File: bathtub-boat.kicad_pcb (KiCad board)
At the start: 2 copper layers, 61 x 35 mm, 54 parts, among them J1 I2C, J2 SPI, J3 I2C, J4 DS18B20, J5 1WireTRS, SW1 MODE, SW2 RESET, SW3 POWER, SW4 A, U1 esp-01m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

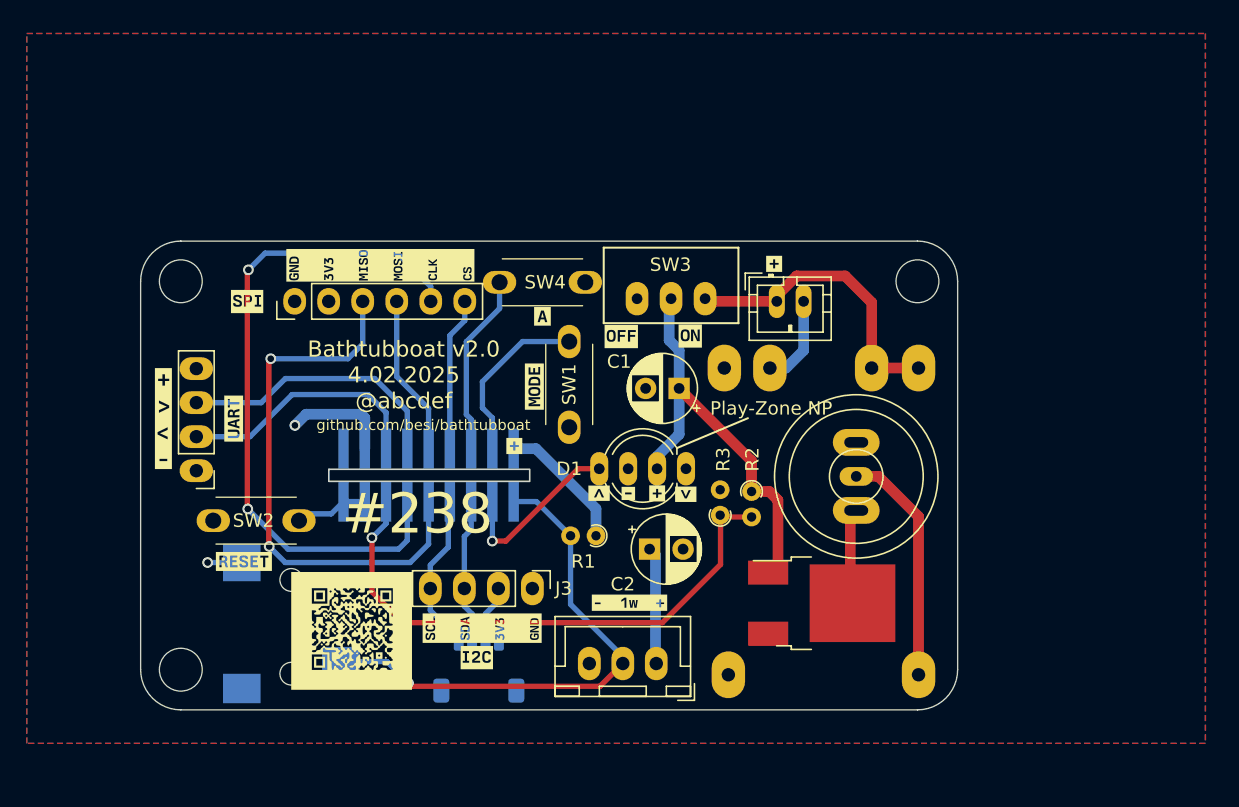
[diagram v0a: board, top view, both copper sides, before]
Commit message: Add a DS18B20 that is facing downwards in the center for under water placement
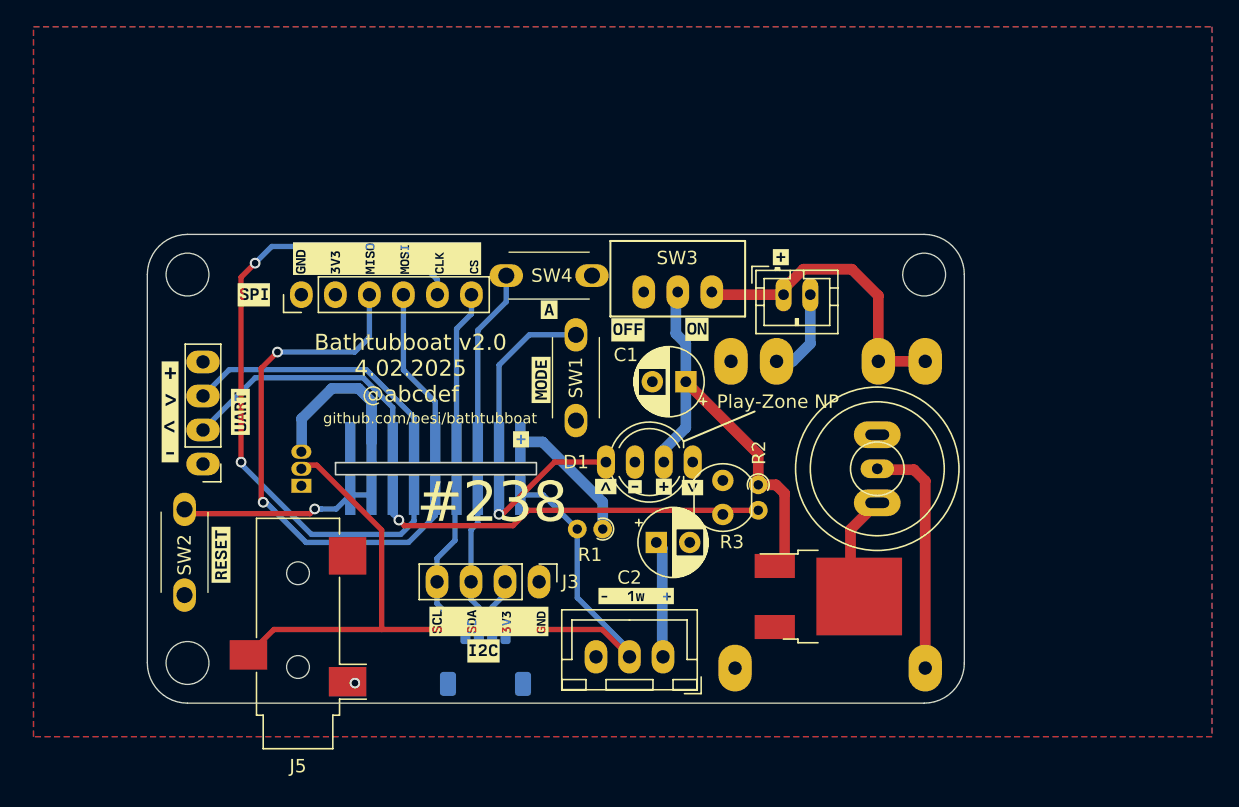
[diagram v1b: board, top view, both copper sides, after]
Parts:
- removed the G*** at (115.3, 94.6)
- added U4: DS18B20, Package_TO_SOT_THT:TO-92_Inline, B.Cu at (111.5, 83.8)
- added kibuzzard-65B8C757: G***, kibuzzard-65B8C757, B.Cu at (130.0, 68.1)
- J5: moved to F.Cu
- R3: value TODO Add Light meter here -> A1050; footprint Resistor_THT:R_Axial_DIN0204_L3.6mm_D1.6mm_P1.90mm_Vertical -> OptoDevice:R_LDR_4.9x4.2mm_P2.54mm_Vertical
- moved kibuzzard-65B79597 7.90 mm to (101.2, 88.8), turned to -90 degrees
- moved SW2 5.96 mm to (102.8, 91.9), turned to 90 degrees
- moved kibuzzard-65B79597 1.78 mm to (105.5, 88.9), turned to 90 degrees
- moved U6 1.67 mm to (154.5, 82.5)
- moved kibuzzard-65B7959E 0.92 mm to (132.0, 75.7), turned to -90 degrees
- moved kibuzzard-65D7C44D 0.75 mm to (107.0, 78.2), turned to -90 degrees
- moved BT3 0.71 mm to (147.5, 69.5)
- moved C1 0.71 mm to (140.2, 76.0)
- moved C2 0.71 mm to (138.0, 88.0)
- moved D1 0.71 mm to (140.7, 82.0)
- moved H1 0.71 mm to (103.0, 68.0)
- moved H2 0.71 mm to (158.0, 68.0)
- moved H3 0.71 mm to (103.0, 97.0)
- moved J1 0.71 mm to (125.2, 96.7)
- moved J2 0.71 mm to (111.5, 69.5)
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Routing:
- net Temp: track 39.0 -> 62.0 mm, vias 1 -> 0
- net ADC: track 42.0 -> 29.6 mm
- net Net-(U1-GP16): track 5.50 -> 14.7 mm, vias 0 -> 1
- net Neopixel: track 13.2 -> 11.1 mm
- net SPI_MISO: track 40.7 -> 38.8 mm
- net GND: track 7.18 -> 8.69 mm, vias 0 -> 1
- net SPI_CLK: track 50.5 -> 49.2 mm
- net +3V3: track 33.7 -> 35.0 mm, vias 2 -> 0
- net Net-(U1-GP0): track 13.0 -> 12.4 mm
- net TX: track 18.7 -> 19.3 mm

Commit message: Change resistors, improve silkscreen and add OSHW logo
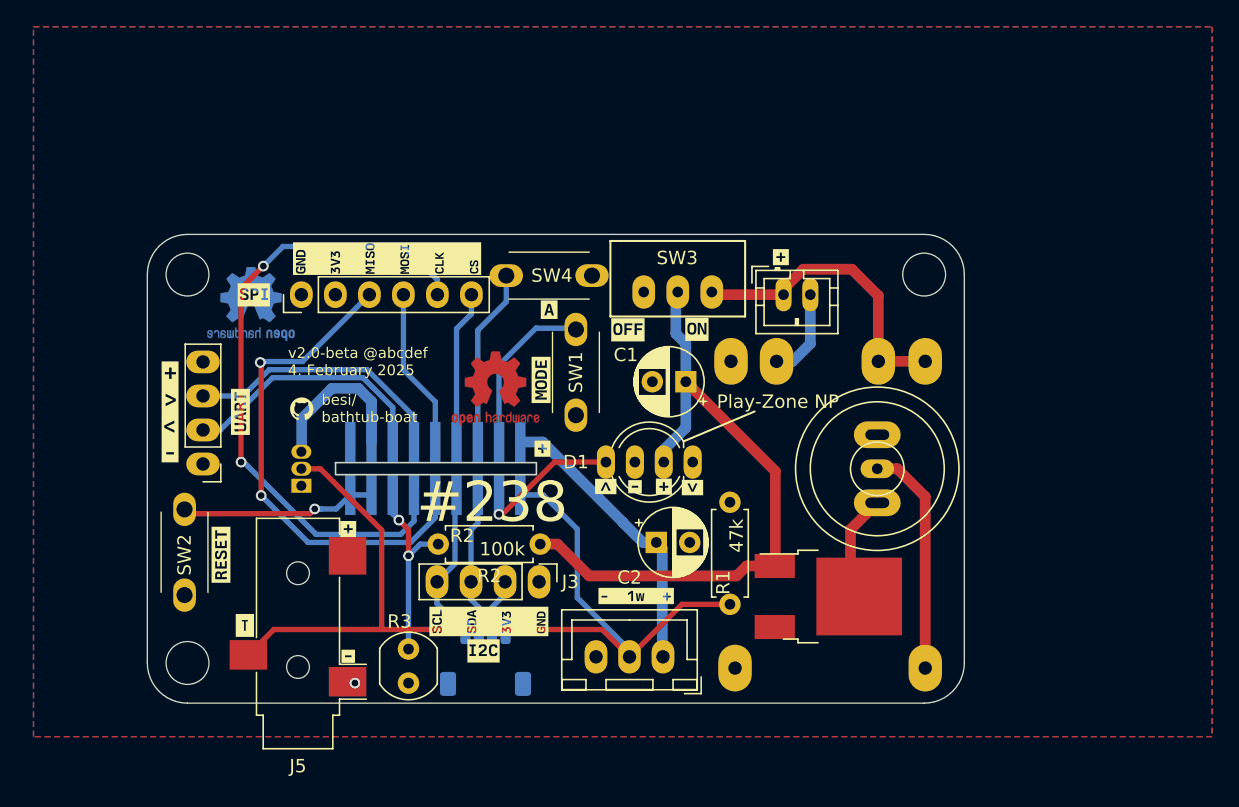
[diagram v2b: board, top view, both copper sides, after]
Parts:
- added G***: LOGO, LOGO, F.Cu at (111.5, 78.0)
- added REF**: OSHW-Logo2_7.3x6mm_Copper, Symbol:OSHW-Logo2_7.3x6mm_Copper, F.Cu at (126.0, 76.5)
- added REF**: OSHW-Logo2_7.3x6mm_Copper, Symbol:OSHW-Logo2_7.3x6mm_Copper, B.Cu at (107.7, 70.2)
- added kibuzzard-65B795B9: G***, kibuzzard-65B795B9, F.Cu at (115.0, 87.0)
- added kibuzzard-65D6F389: G***, kibuzzard-65D6F389, F.Cu at (115.0, 96.5)
- added kibuzzard-67A2929D: G***, kibuzzard-67A2929D, F.Cu at (107.3, 94.2)
- R1, R2: footprint Resistor_THT:R_Axial_DIN0204_L3.6mm_D1.6mm_P1.90mm_Vertical -> Resistor_THT:R_Axial_DIN0207_L6.3mm_D2.5mm_P7.62mm_Horizontal
- moved R3 25.5 mm to (119.5, 96.0), turned to -90 degrees
- moved R2 16.9 mm to (129.3, 88.1), turned to 180 degrees
- moved R1 9.71 mm to (143.5, 85.0), turned to -90 degrees
- moved kibuzzard-65B795B9 1.75 mm to (129.5, 81.0)
- moved kibuzzard-65B7959E 0.54 mm to (132.0, 75.2)
- moved SW1 0.40 mm to (132.0, 78.5)
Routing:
- net +5V: track 31.9 -> 49.3 mm
- net ADC: track 29.6 -> 14.6 mm, vias 1 -> 2
- net Temp: track 62.0 -> 71.0 mm
- net +3V3: track 35.0 -> 38.2 mm
- net SPI_MISO: track 38.8 -> 37.1 mm
- net VBUS: track 17.9 -> 17.2 mm
- net SPI_CLK: track 49.2 -> 48.6 mm
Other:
- board text added: "besi/ bathtub-boat"
- board text added: "v2.0-beta @abcdef 4. February 2025"
- board text removed: "Bathtubboat v2.0 4.02.2025 @abcdef"
- board text removed: "github.com/besi/bathtubboat"

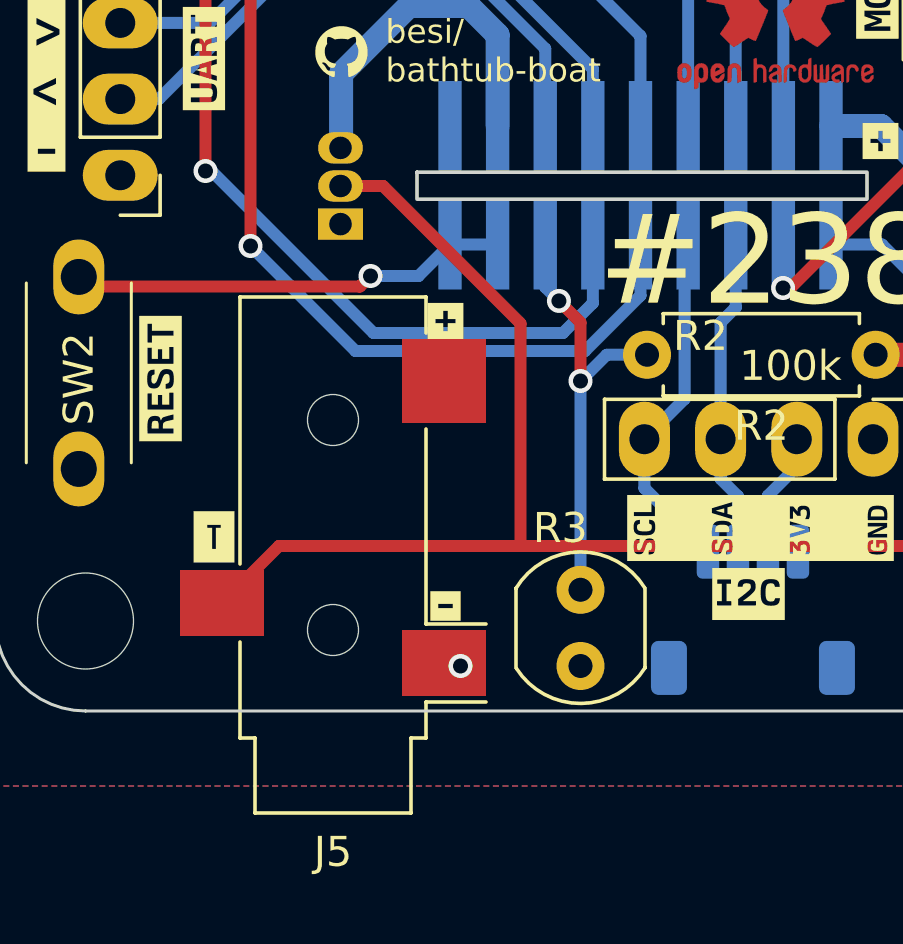
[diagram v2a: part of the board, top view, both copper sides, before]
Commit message: Final tweaks prior to production
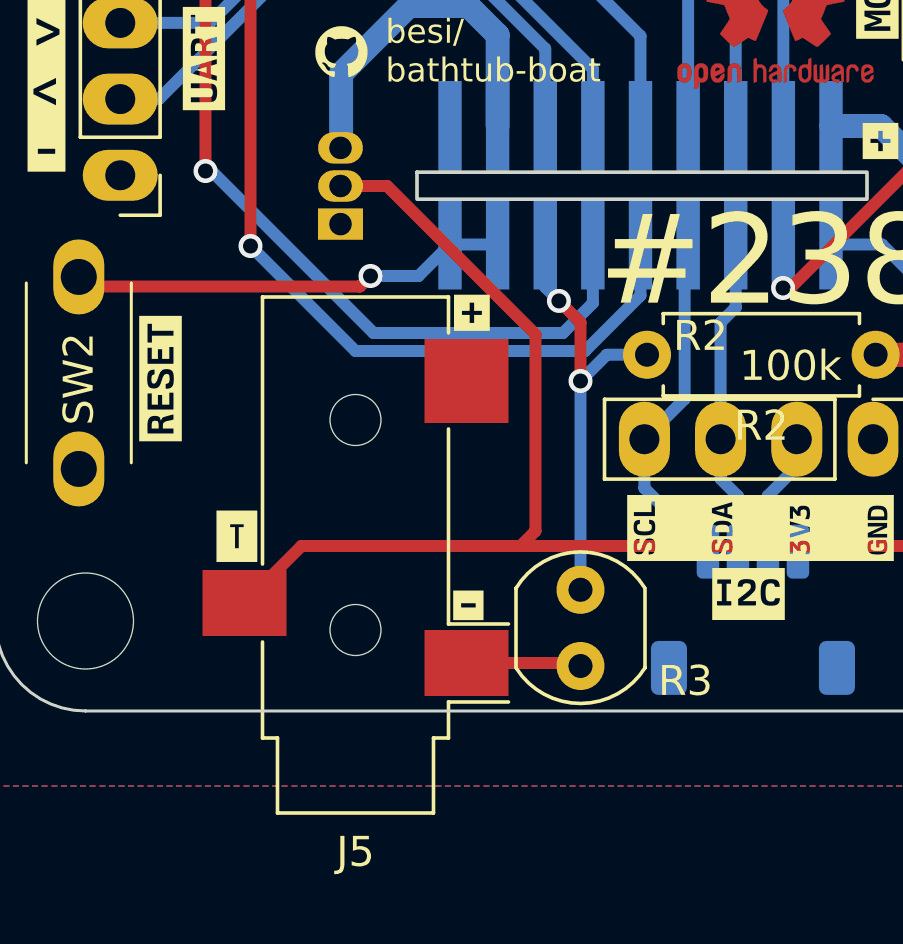
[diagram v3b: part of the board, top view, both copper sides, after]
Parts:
- moved kibuzzard-65B795B9 0.92 mm to (115.9, 86.7)
- moved kibuzzard-65D6F389 0.76 mm to (115.8, 96.5)
- moved kibuzzard-67A2929D 0.76 mm to (108.0, 94.2)
- moved J5 0.75 mm to (112.0, 94.8)
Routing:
- net GND: track 8.69 -> 12.2 mm, vias 1 -> 0
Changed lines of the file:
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@@
   )
   (footprint "kibuzzard-67A2929D" (layer "F.Cu")
-    (at 107.283544 94.196962)
+    (at 108.046676 94.175651)
     (descr "Generated with KiBuzzard")
     (tags "kb_params=eyJBbGlnbm1lbnRDaG9pY2UiOiAiUmlnaHQiLCAiQ2FwTGVmdENob2ljZSI6ICJbIiwgIkNhcFJpZ2h0Q2hvaWNlIjogIl0iLCAiRm9udENvbWJvQm94IjogIm1wbHVzLTFtbi1tZWRpdW0iLCAiSGVpZ2h0Q3RybCI6IDAuOCwgIkxheWVyQ29tYm9Cb3giOiAiRi5TaWxrUyIsICJMaW5lU3BhY2luZ0N0cmwiOiAxLjUsICJNdWx0aUxpbmVUZXh0IjogIlQiLCAiUGFkZGluZ0JvdHRvbUN0cmwiOiA1LjAsICJQYWRkaW5nTGVmdEN0cmwiOiA1LjAsICJQYWRkaW5nUmlnaHRDdHJsIjogNS4wLCAiUGFkZGluZ1RvcEN0cmwiOiA1LjAsICJXaWR0aEN0cmwiOiAwLjAsICJhZHZhbmNlZENoZWNrYm94IjogZmFsc2UsICJpbmxpbmVGb3JtYXRUZXh0Ym94IjogZmFsc2UsICJsaW5lb3ZlclN0eWxlQ2hvaWNlIjogIlNxdWFyZSIsICJsaW5lb3ZlclRoaWNrbmVzc0N0cmwiOiAxfQ==")
@@
   )
   (footprint "kibuzzard-65B795B9" (layer "F.Cu")
-    (at 115 87 180)
+    (at 115.87993 86.726043 180)
     (descr "Generated with KiBuzzard")
     (tags "kb_params=eyJBbGlnbm1lbnRDaG9pY2UiOiAiUmlnaHQiLCAiQ2FwTGVmdENob2ljZSI6ICJbIiwgIkNhcFJpZ2h0Q2hvaWNlIjogIl0iLCAiRm9udENvbWJvQm94IjogIkJlcmtlbGV5TW9uby1Cb2xkIiwgIkhlaWdodEN0cmwiOiAiLjgiLCAiTGF5ZXJDb21ib0JveCI6ICJGLlNpbGtTIiwgIk11bHRpTGluZVRleHQiOiAiKyIsICJQYWRkaW5nQm90dG9tQ3RybCI6ICI1IiwgIlBhZGRpbmdMZWZ0Q3RybCI6ICI1IiwgIlBhZGRpbmdSaWdodEN0cmwiOiAiNSIsICJQYWRkaW5nVG9wQ3RybCI6ICI1IiwgIldpZHRoQ3RybCI6ICIifQ==")
@@
     (property "ki_keywords" "light dependent photo resistor LDR")
     (attr through_hole)
-    (fp_text reference "R3" (at -2.057608 0.672931) (layer "F.SilkS")
+    (fp_text reference "R3" (at 3.04 -3.5) (layer "F.SilkS")
         (effects (font (size 1 1) (thickness 0.15)))
     )
@@
   )
   (footprint "kibuzzard-65D6F389" (layer "F.Cu")
-    (at 115 96.5)
+    (at 115.763132 96.478689)
     (descr "Generated with KiBuzzard")
     (tags "kb_params=eyJBbGlnbm1lbnRDaG9pY2UiOiAiUmlnaHQiLCAiQ2FwTGVmdENob2ljZSI6ICJbIiwgIkNhcFJpZ2h0Q2hvaWNlIjogIl0iLCAiRm9udENvbWJvQm94IjogIkJlcmtlbGV5TW9uby1Cb2xkIiwgIkhlaWdodEN0cmwiOiAiLjgiLCAiTGF5ZXJDb21ib0JveCI6ICJGLlNpbGtTIiwgIk11bHRpTGluZVRleHQiOiAiLSIsICJQYWRkaW5nQm90dG9tQ3RybCI6ICI4IiwgIlBhZGRpbmdMZWZ0Q3RybCI6ICI1IiwgIlBhZGRpbmdSaWdodEN0cmwiOiAiNSIsICJQYWRkaW5nVG9wQ3RybCI6ICI4IiwgIldpZHRoQ3RybCI6ICIifQ==")
@@
   )
   (footprint "Connector_Audio:Jack_3.5mm_CUI_SJ-3523-SMT_Horizontal" (layer "F.Cu")
-    (at 111.25 94.8 180)
+    (at 112 94.8 180)
     (descr "3.5 mm, Stereo, Right Angle, Surface Mount (SMT), Audio Jack Connector (https://www.cui.com/product/resource/sj-352x-smt-series.pdf)")
     (tags "3.5mm audio cui horizontal jack stereo")
@@
     (style (thickness 0.15) (arrow_length 1.27) (text_position_mode 0) (extension_height 0.58642) (extension_offset 0.5) keep_text_aligned)
   )
-  (segment (start 115.4 98.4) (end 115.5 98.5) (width 0.4) (layer "F.Cu") (net 1))
+  (segment (start 119.4 98.4) (end 119.5 98.5) (width 0.4) (layer "F.Cu") (net 1))
+  (segment (start 115.7 98.4) (end 119.4 98.4) (width 0.4) (layer "F.Cu") (net 1))
+  (segment (start 115.6 98.5) (end 115.5 98.5) (width 0.4) (layer "F.Cu") (net 1))
   (segment (start 153.149673 92.036992) (end 152.5 91.387319) (width 0.8) (layer "F.Cu") (net 1))
-  (segment (start 114.95 98.4) (end 115.4 98.4) (width 0.4) (layer "F.Cu") (net 1))
+  (segment (start 115.7 98.4) (end 115.6 98.5) (width 0.4) (layer "F.Cu") (net 1))
   (segment (start 152.5 91.387319) (end 152.5 87.039021) (width 0.8) (layer "F.Cu") (net 1))
   (segment (start 152.5 87.039021) (end 154.5 85.039021) (width 0.8) (layer "F.Cu") (net 1))
-  (via (at 115.5 98.5) (size 0.8) (drill 0.5) (layers "F.Cu" "B.Cu") (net 1))
   (segment (start 140.419 81.419) (end 140.5 81.5) (width 0.4) (layer "B.Cu") (net 2))
   (segment (start 116.7375 77.4675) (end 115.77 76.5) (width 0.8) (layer "B.Cu") (net 3))
@@
   (segment (start 147.5 69.5) (end 142.341938 69.5) (width 0.8) (layer "F.Cu") (net 19))
   (segment (start 152.6 67.6) (end 148.982233 67.6) (width 0.8) (layer "F.Cu") (net 19))
-  (segment (start 117.5 87.08) (end 117.5 94.5) (width 0.4) (layer "F.Cu") (net 20))
-  (segment (start 109.45 94.5) (end 107.55 96.4) (width 0.4) (layer "F.Cu") (net 20))
+  (segment (start 110.2 94.5) (end 108.3 96.4) (width 0.4) (layer "F.Cu") (net 20))
+  (segment (start 111.5 82.5) (end 113.055465 82.5) (width 0.4) (layer "F.Cu") (net 20))
+  (segment (start 113.055465 82.5) (end 118 87.444535) (width 0.4) (layer "F.Cu") (net 20))
+  (segment (start 117.5 94.5) (end 110.2 94.5) (width 0.4) (layer "F.Cu") (net 20))
+  (segment (start 118 94) (end 117.5 94.5) (width 0.4) (layer "F.Cu") (net 20))
   (segment (start 136 96.54) (end 133.96 94.5) (width 0.4) (layer "F.Cu") (net 20))
-  (segment (start 117.5 94.5) (end 109.45 94.5) (width 0.4) (layer "F.Cu") (net 20))
   (segment (start 139.92 92.62) (end 143.5 92.62) (width 0.4) (layer "F.Cu") (net 20))
   (segment (start 133.96 94.5) (end 117.5 94.5) (width 0.4) (layer "F.Cu") (net 20))
-  (segment (start 112.92 82.5) (end 117.5 87.08) (width 0.4) (layer "F.Cu") (net 20))
-  (segment (start 111.5 82.5) (end 112.92 82.5) (width 0.4) (layer "F.Cu") (net 20))
   (segment (start 136 96.54) (end 139.92 92.62) (width 0.4) (layer "F.Cu") (net 20))
+  (segment (start 118 87.444535) (end 118 94) (width 0.4) (layer "F.Cu") (net 20))
   (segment (start 132.1 87) (end 129.55 84.45) (width 0.4) (layer "B.Cu") (net 20))
   (segment (start 132.1 92.123705) (end 136 96.023705) (width 0.4) (layer "B.Cu") (net 20))
